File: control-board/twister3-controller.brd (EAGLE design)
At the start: 191 x 90.5 mm, 56 parts, among them J1 BARREL-JACK_PJ-063BH, J5 OSTVN04A150, U1 IS31FL3193, U2 MIC4680-5.0YM-TR, U3 MAX6816, U4 TMC2130-LA, U5 Teensy 3.2, U6 GDM1602K

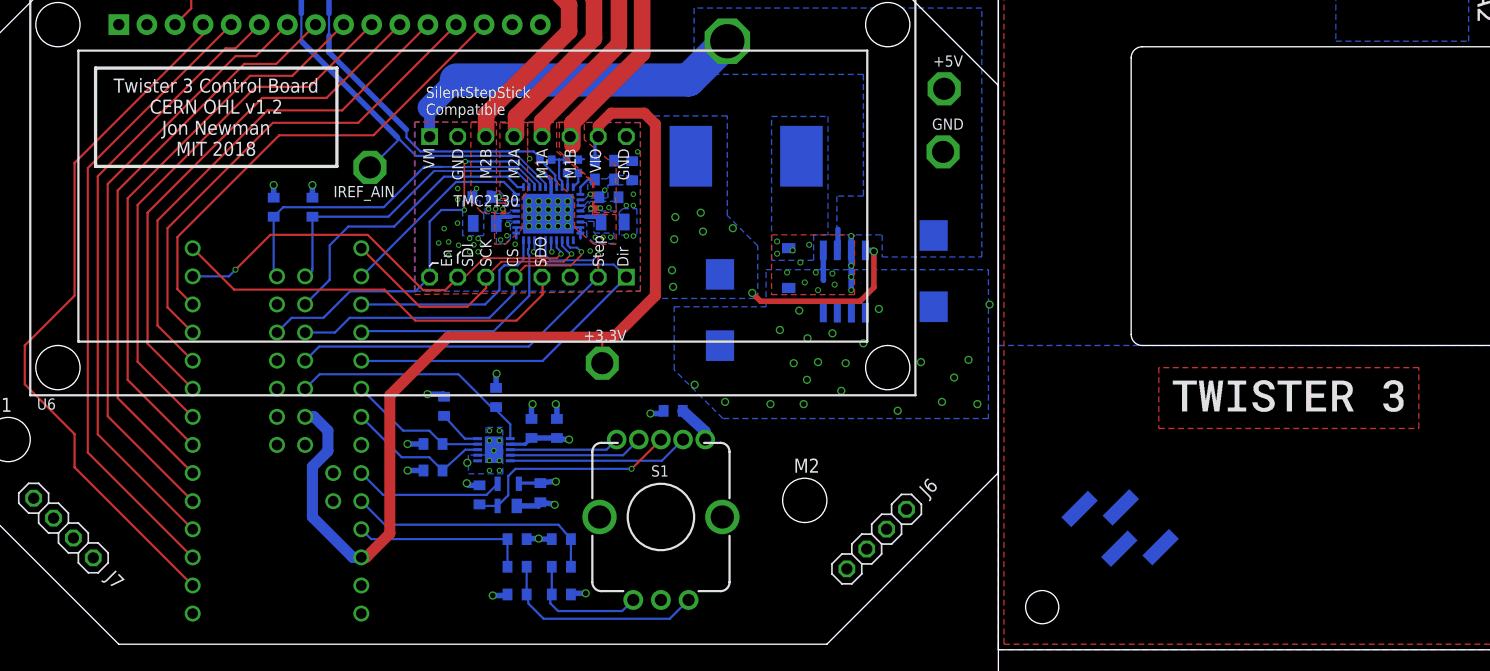
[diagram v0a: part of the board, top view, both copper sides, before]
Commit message: Added oe-logo and Twister 3 to tstop on front panel
- Reduced the both bcream and bstop for the SMD threaded inserts to 3.2
mm on bottom on front panel
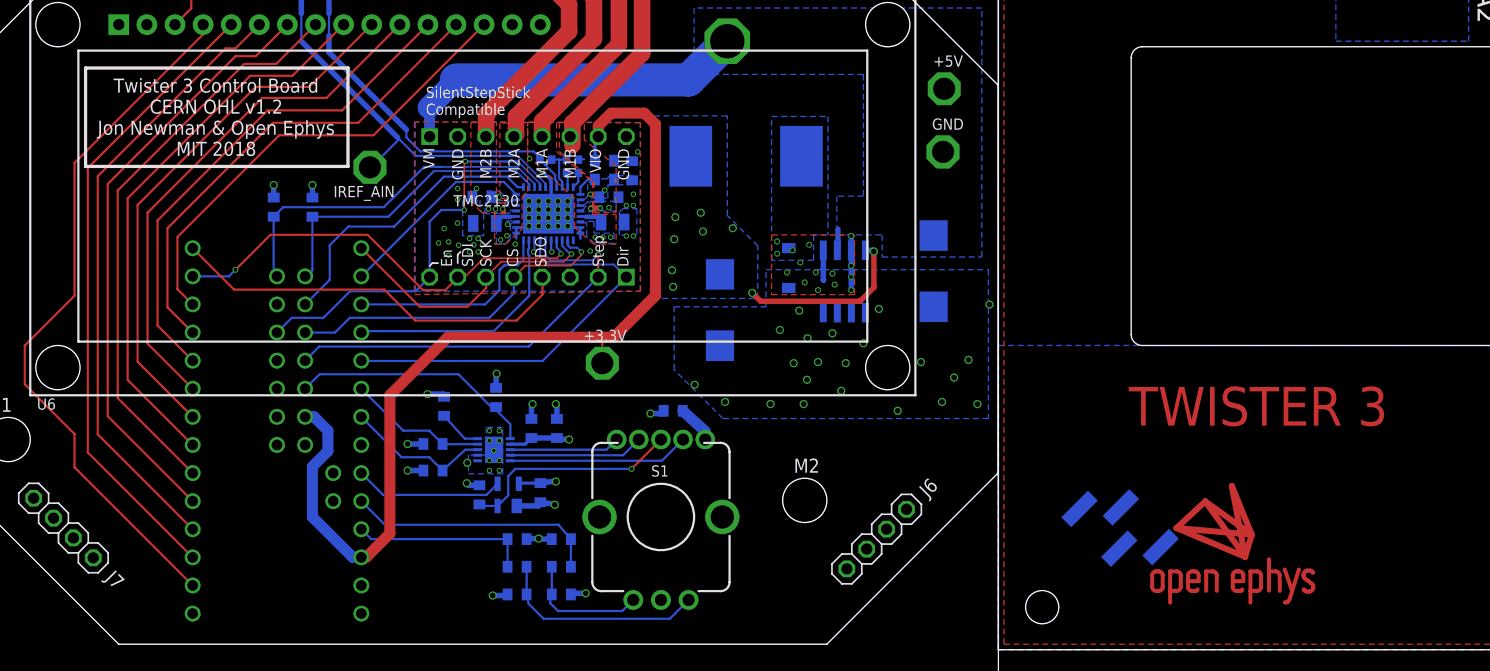
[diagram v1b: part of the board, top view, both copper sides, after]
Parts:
- added X1: OE-LOGO_14X10, jonnew:OE-LOGO-14X10
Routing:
- removed copper zone on layer 1, net N$13
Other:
- board text added: "TWISTER 3"
- board text added: "Twister 3 Control Board CERN OHL v1.2 Jon Newman & Open Ephys MIT 2018"
- board text removed: "Twister 3 Control Board CERN OHL v1.2 Jon Newman MIT 2018"

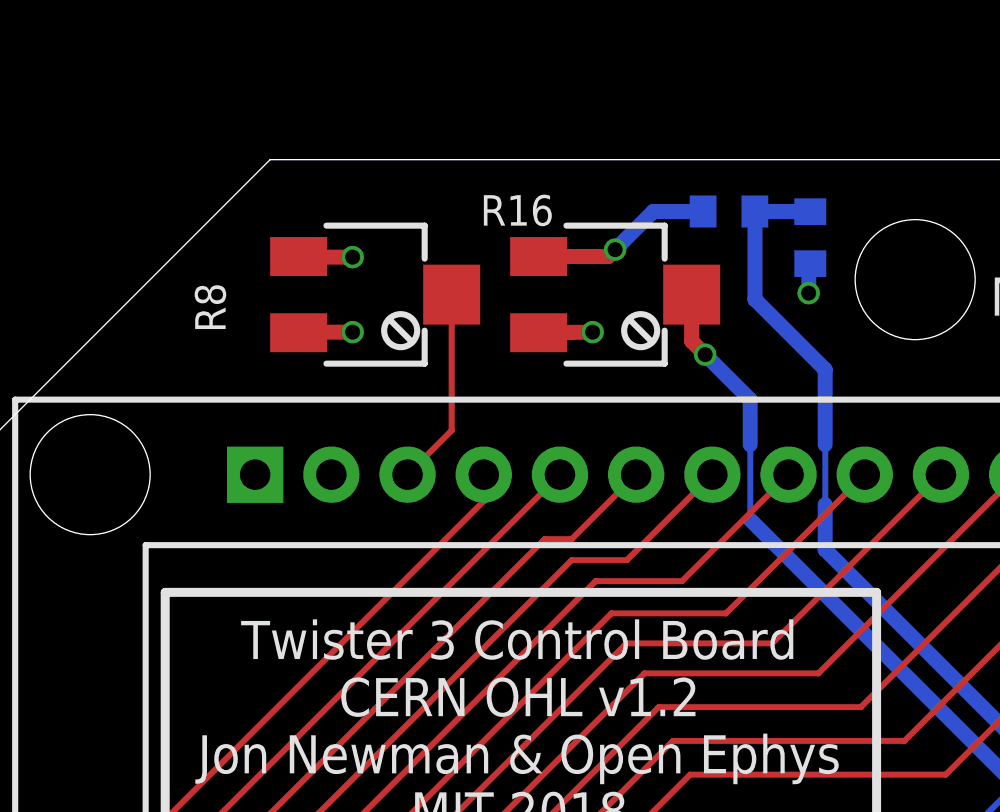
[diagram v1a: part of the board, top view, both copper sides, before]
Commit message: Move potentiometers to bottom of board
- This will cut down on production costs since they are not available
through the front panel anyway
- Alternative, hard-coded resistor (not populated) for LCD bias
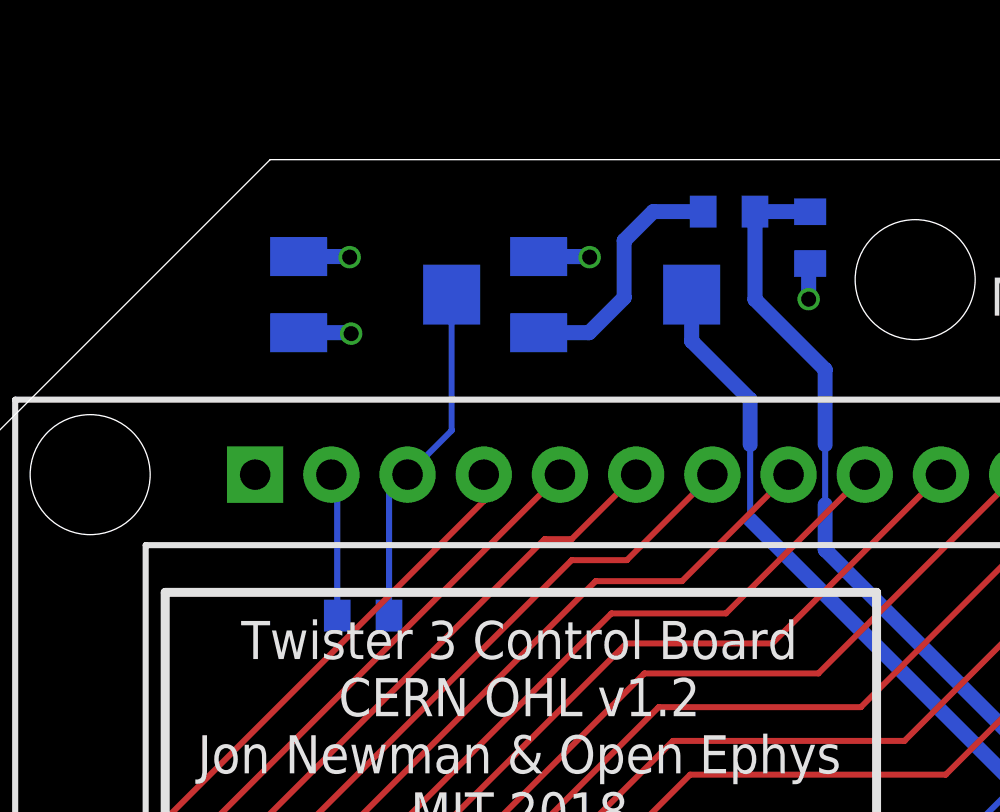
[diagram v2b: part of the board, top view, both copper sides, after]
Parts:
- added R18: DNP, jonnew:0603
- flipped R16 to the bottom, turned to 90 degrees
- flipped R8 to the bottom, turned to 90 degrees
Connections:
- net +5V0: now also R18.1
- net N$11: now also R18.2
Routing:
- net +5V0: track 40.2 -> 45.0 mm
- net N$11: track 7.13 -> 11.6 mm
- net VREF2: track 6.10 -> 8.27 mm, vias 1 -> 0
- net IREF: vias 1 -> 0
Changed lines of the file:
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@@
 <setting verticaltext="up"/>
 </settings>
-<grid distance="1" unitdist="mm" unit="mm" style="lines" multiple="1" display="yes" altdistance="5" altunitdist="mil" altunit="mil"/>
+<grid distance="0.1" unitdist="mm" unit="mm" style="lines" multiple="1" display="yes" altdistance="5" altunitdist="mil" altunit="mil"/>
 <layers>
 <layer number="1" name="Top" color="4" fill="1" visible="yes" active="yes"/>
@@
 <attribute name="VALUE" x="47.29" y="13" size="1.016" layer="28" font="vector" ratio="19" rot="MR0" align="center-left"/>
 </element>
-<element name="R8" library="jonnew" package="SM-42/43X" value="20k" x="20" y="62.5" locked="yes" smashed="yes" rot="R270">
-<attribute name="NAME" x="14" y="62.9" size="1.016" layer="25" font="vector" ratio="19" rot="R270"/>
-<attribute name="VALUE" x="15.2" y="63" size="1.016" layer="27" font="vector" ratio="19" rot="R270"/>
+<element name="R8" library="jonnew" package="SM-42/43X" value="20k" x="20" y="62.5" locked="yes" smashed="yes" rot="MR90">
+<attribute name="NAME" x="14" y="62.1" size="1.016" layer="26" font="vector" ratio="19" rot="MR90"/>
+<attribute name="VALUE" x="15.2" y="62" size="1.016" layer="28" font="vector" ratio="19" rot="MR90"/>
 </element>
 <element name="R5" library="jonnew" package="0603" value="10k" x="52" y="7.5" smashed="yes" rot="MR0">
@@
 <attribute name="VALUE" x="92.84" y="27.85" size="1.016" layer="28" font="vector" ratio="19" rot="MR90"/>
 </element>
-<element name="R16" library="jonnew" package="SM-42/43X" value="20k" x="28" y="62.5" locked="yes" smashed="yes" rot="R270">
-<attribute name="NAME" x="23.5" y="64.8" size="1.016" layer="25" font="vector" ratio="19"/>
-<attribute name="VALUE" x="24.5" y="59.3" size="1.016" layer="27" font="vector" ratio="19"/>
+<element name="R16" library="jonnew" package="SM-42/43X" value="20k" x="28" y="62.5" locked="yes" smashed="yes" rot="MR90">
+<attribute name="NAME" x="23.5" y="60.2" size="1.016" layer="26" font="vector" ratio="19" rot="MR180"/>
+<attribute name="VALUE" x="24.5" y="65.7" size="1.016" layer="28" font="vector" ratio="19" rot="MR180"/>
 </element>
 <element name="J5" library="jonnew" package="1X04" value="OSTVN04A150" x="143.5" y="63" smashed="yes">
@@
 </element>
 <element name="X1" library="jonnew" package="OE-LOGO-14X10" value="OE-LOGO_14X10" x="116" y="8"/>
+<element name="R18" library="jonnew" package="0603" value="DNP" x="19.6" y="51.8" smashed="yes" rot="MR180">
+<attribute name="DK" value="PxxxxHTR-ND" x="19.6" y="51.8" size="1.778" layer="28" rot="MR180" display="off"/>
+<attribute name="MN" value="Panasonic" x="19.6" y="51.8" size="1.778" layer="28" rot="MR180" display="off"/>
+<attribute name="MPN" value="ERJ-3EKFxxxxV" x="19.6" y="51.8" size="1.778" layer="28" rot="MR180" display="off"/>
+<attribute name="NAME" x="17.497" y="52.297" size="1.016" layer="26" font="vector" ratio="18" rot="MR180" align="center-right"/>
+<attribute name="VALUE" x="17.5" y="51.1" size="1.016" layer="28" font="vector" ratio="18" rot="MR0" align="center-left"/>
+</element>
 </elements>
 <signals>
@@
 <via x="75.75" y="28.9" extent="1-16" drill="0.5"/>
 <via x="78.25" y="28.15" extent="1-16" drill="0.5"/>
-<via x="19.25" y="61.25" extent="1-16" drill="0.5"/>
-<via x="27.25" y="61.25" extent="1-16" drill="0.5"/>
-<wire x1="25.5" y1="61.23" x2="26.55" y2="61.23" width="0.5" layer="1"/>
-<wire x1="25.27" y1="61.23" x2="27.25" y2="61.25" width="0.5" layer="1"/>
+<via x="27.15" y="63.75" extent="1-16" drill="0.5"/>
 <via x="53.95" y="10.05" extent="1-16" drill="0.5"/>
 <wire x1="52.8636" y1="10" x2="53.0914" y2="10.05" width="0.5" layer="16"/>
@@
 <contactref element="R14" pad="1"/>
 <contactref element="R15" pad="1"/>
-<wire x1="19.25" y1="61.25" x2="17.45" y2="61.25" width="0.5" layer="1"/>
-<wire x1="17.45" y1="61.25" x2="17.45" y2="61.23" width="0.5" layer="1"/>
-<wire x1="25.45" y1="61.23" x2="25.5" y2="61.23" width="0.3" layer="1"/>
-<wire x1="25.45" y1="61.23" x2="25.27" y2="61.23" width="0.3" layer="1"/>
 <contactref element="GND" pad="1"/>
-<via x="34.45" y="62.55" extent="1-16" drill="0.5"/>
-<wire x1="34.45" y1="62.55" x2="34.45" y2="63.4864" width="0.5" layer="16"/>
+<via x="34.45" y="62.35" extent="1-16" drill="0.5"/>
+<wire x1="34.45" y1="62.35" x2="34.45" y2="63.4864" width="0.5" layer="16"/>
 <wire x1="34.45" y1="63.4864" x2="34.5" y2="63.5364" width="0.5" layer="16"/>
 <via x="53.1345" y="44.385" extent="1-16" drill="0.3"/>
@@
 <wire x1="55.0452" y1="42.28734375" x2="55.074" y2="42.25854375" width="0.3" layer="16"/>
 <wire x1="55.074" y1="42.25854375" x2="55.074" y2="41.56" width="0.3" layer="16"/>
+<wire x1="26.88641875" y1="63.77" x2="25.45" y2="63.77" width="0.5" layer="16"/>
+<wire x1="25.45" y1="63.77" x2="27.13" y2="63.77" width="0.5" layer="16"/>
+<wire x1="27.13" y1="63.77" x2="27.15" y2="63.75" width="0.5" layer="16"/>
+<via x="19.15" y="63.75" extent="1-16" drill="0.5"/>
+<wire x1="17.45" y1="63.77" x2="19.13" y2="63.77" width="0.5" layer="16"/>
+<wire x1="19.13" y1="63.77" x2="19.15" y2="63.75" width="0.5" layer="16"/>
 </signal>
 <signal name="ENC_A">
@@
 <contactref element="U6" pad="3"/>
 <contactref element="R8" pad="2"/>
-<wire x1="21.45" y1="56.87" x2="21.08" y2="56.5" width="0.2" layer="1"/>
-<wire x1="21.08" y1="56.5" x2="22.55" y2="57.97" width="0.2032" layer="1"/>
-<wire x1="22.55" y1="57.97" x2="22.55" y2="62.5" width="0.2032" layer="1"/>
+<wire x1="22.55" y1="62.5" x2="22.55" y2="57.97" width="0.2032" layer="16"/>
+<contactref element="R18" pad="2"/>
+<wire x1="21.08" y1="56.5" x2="22.55" y2="57.97" width="0.2032" layer="16"/>
+<wire x1="20.4636" y1="51.8" x2="20.4636" y2="55.8836" width="0.2032" layer="16"/>
+<wire x1="20.4636" y1="55.8836" x2="21.08" y2="56.5" width="0.2032" layer="16"/>
 </signal>
 <signal name="RS">
@@
 <wire x1="41.2" y1="46.3" x2="32.5" y2="55" width="0.5" layer="16"/>
 <wire x1="32.5" y1="55" x2="32.5" y2="57.5" width="0.2" layer="16"/>
-<via x="31" y="60.5" extent="1-16" drill="0.5"/>
 <wire x1="46.7" y1="44.6341" x2="46.7" y2="44.6" width="0.2" layer="16"/>
 <wire x1="46.7" y1="44.6341" x2="42.8659" y2="44.6341" width="0.2" layer="16"/>
@@
 <wire x1="54.574" y1="42.13171875" x2="52.07161875" y2="44.6341" width="0.16" layer="16"/>
 <wire x1="32.5" y1="57.5" x2="32.5" y2="59" width="0.5" layer="16"/>
-<wire x1="32.5" y1="59" x2="31" y2="60.5" width="0.5" layer="16"/>
-<wire x1="31" y1="60.5" x2="30.55" y2="60.95" width="0.5" layer="1"/>
-<wire x1="30.55" y1="60.95" x2="30.55" y2="62.5" width="0.5" layer="1"/>
+<wire x1="30.55" y1="60.95" x2="30.55" y2="62.5" width="0.5" layer="16"/>
 <contactref element="IREF_AIN" pad="1"/>
 <wire x1="38.7" y1="43.6" x2="38.870709375" y2="43.670709375" width="0.2" layer="16" curve="44.999476"/>
 <wire x1="38.870709375" y1="43.670709375" x2="41.35" y2="46.15" width="0.2" layer="16"/>
+<wire x1="32.5" y1="59" x2="30.55" y2="60.95" width="0.5" layer="16"/>
 </signal>
 <signal name="CFG-6">
@@
 <contactref element="R13" pad="1"/>
 <contactref element="R16" pad="1"/>
-<via x="28" y="64" extent="1-16" drill="0.5"/>
-<wire x1="30.9324" y1="65.269" x2="29.269" y2="65.269" width="0.5" layer="16"/>
-<wire x1="29.269" y1="65.269" x2="28" y2="64" width="0.5" layer="16"/>
-<wire x1="28" y1="64" x2="27.77" y2="63.77" width="0.5" layer="1"/>
-<wire x1="27.77" y1="63.77" x2="25.45" y2="63.77" width="0.5" layer="1"/>
+<wire x1="29.269" y1="65.269" x2="30.9324" y2="65.269" width="0.5" layer="16"/>
+<wire x1="25.45" y1="61.23" x2="27.13" y2="61.23" width="0.5" layer="16"/>
+<wire x1="27.13" y1="61.23" x2="28.3" y2="62.4" width="0.5" layer="16"/>
+<wire x1="28.3" y1="62.4" x2="28.3" y2="64.3" width="0.5" layer="16"/>
+<wire x1="28.3" y1="64.3" x2="29.269" y2="65.269" width="0.5" layer="16"/>
 </signal>
 <signal name="SPI_MODE">
@@
 <via x="33.5" y="42" extent="1-16" drill="0.5"/>
 <wire x1="33.5" y1="42" x2="33.5" y2="40.8636" width="0.5" layer="16"/>
-<via x="19.25" y="63.75" extent="1-16" drill="0.5"/>
+<via x="19.2" y="61.2" extent="1-16" drill="0.5"/>
 <via x="42.1" y="18.6" extent="1-16" drill="0.5"/>
 <via x="42.1" y="16.2" extent="1-16" drill="0.5"/>
@@
 <wire x1="43.9" y1="23.1" x2="45.3414" y2="23.1" width="0.5" layer="16"/>
 <wire x1="45.3414" y1="23.1" x2="45.4" y2="22.8636" width="0.5" layer="16"/>
-<wire x1="19.25" y1="63.75" x2="17.45" y2="63.75" width="0.5" layer="1"/>
-<wire x1="17.45" y1="63.75" x2="17.45" y2="63.77" width="0.5" layer="1"/>
 <wire x1="51.385" y1="18.58" x2="52.7436" y2="18.58" width="0.3" layer="16"/>
 <wire x1="52.7436" y1="18.58" x2="53.3" y2="19.1364" width="0.3" layer="16"/>
@@
 <wire x1="52.2236" y1="15.0636" x2="52.16" y2="15" width="0.3" layer="16"/>
 <contactref element="+5V" pad="1"/>
+<contactref element="R18" pad="1"/>
+<wire x1="17.45" y1="61.23" x2="19.17" y2="61.23" width="0.5" layer="16"/>
+<wire x1="19.17" y1="61.23" x2="19.2" y2="61.2" width="0.5" layer="16"/>
+<wire x1="18.7364" y1="51.8" x2="18.7364" y2="56.3036" width="0.2032" layer="16"/>
+<wire x1="18.7364" y1="56.3036" x2="18.54" y2="56.5" width="0.2032" layer="16"/>
 </signal>
 <signal name="V_BM">
